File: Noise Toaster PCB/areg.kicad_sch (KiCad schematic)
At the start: 18 parts, among them Q1 2N3906, Q9 2N5457, U2 LM324

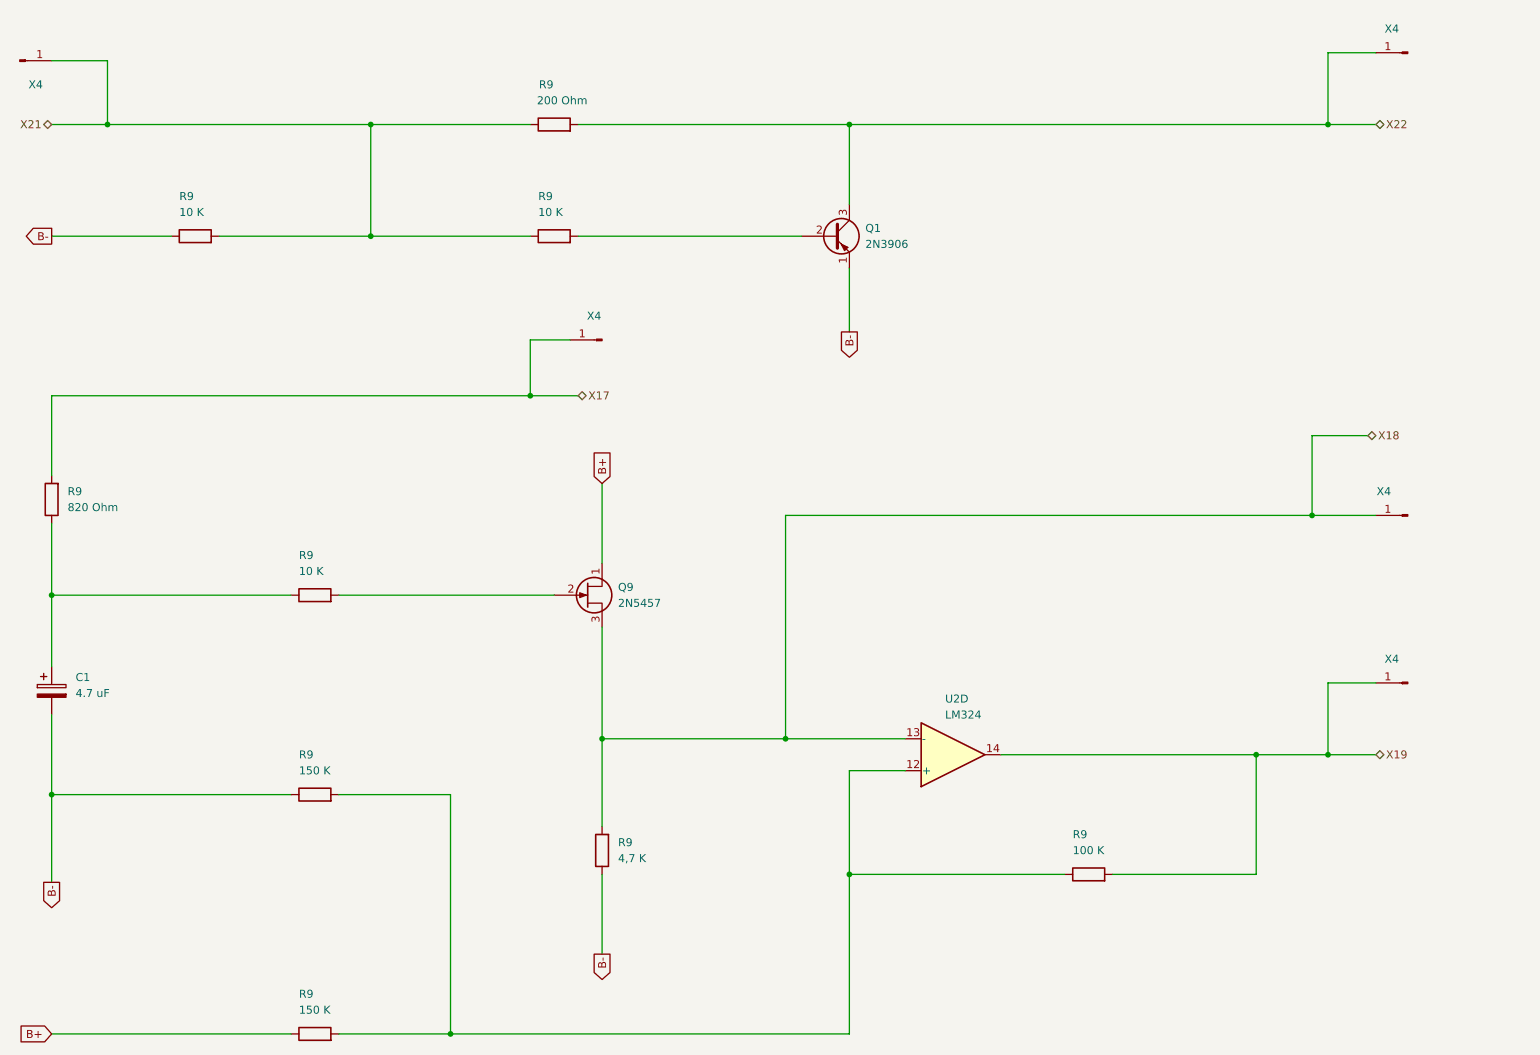
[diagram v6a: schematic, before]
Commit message: changed header pins to groups
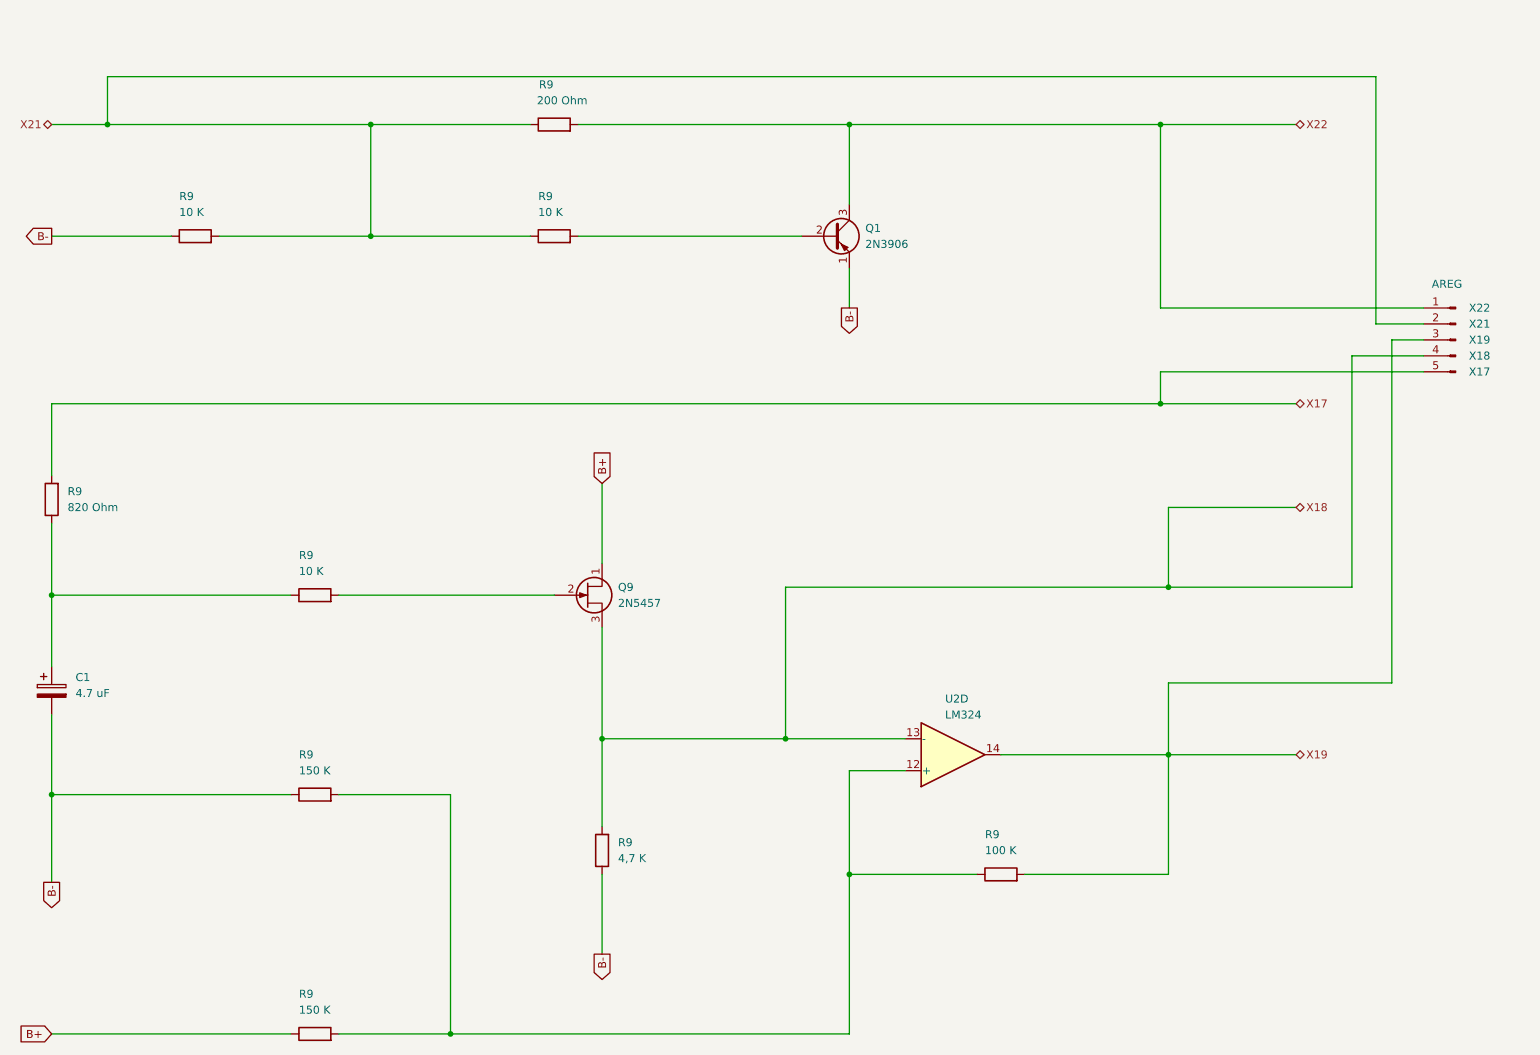
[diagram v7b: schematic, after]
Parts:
- removed X4 (x5): ~, Connector_PinHeader_1.00mm:PinHeader_1x01_P1.00mm_Vertical, symbol Connector:Conn_01x01_Pin
- added J3: AREG, Connector_PinHeader_2.00mm:PinHeader_1x05_P2.00mm_Vertical, symbol Connector:Conn_01x05_Pin
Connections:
- net X17: now also J3.5 (Pin_5)
- net X18: now also J3.4 (Pin_4)
- net X19: now also J3.3 (Pin_3)
- net X21: now also J3.2 (Pin_2)
- net X22: now also J3.1 (Pin_1)
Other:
- moved on the sheet: R9
